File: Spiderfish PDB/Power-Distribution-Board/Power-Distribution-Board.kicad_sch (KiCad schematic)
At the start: 20 parts, among them J1 USB_B_Micro, J2 Conn_01x04_Pin, SW1 SW_Push, SW2 SW_SPDT, U1 STM32L052K6T6, U2 AOZ2264NQI-11

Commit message: added all regulators
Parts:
- added C10, C7: 330u, symbol Device:C
- added C11, C8: 10n, symbol Device:C
- added C12, C13, C14, C15, C16, C17, C18, C19, C20, C21, C22, C23, C24, C25, C26, C27, C28, C29, C30, C31: C, symbol Device:C
- added C6, C9: 100u, symbol Device:C
- added D1, D2: SK32, symbol Device:D
- added L2, L3: 33u, symbol Device:L
- added L4, L5, L6, L7, L8: L, symbol Device:L
- added R10, R12: 10k, symbol Device:R
- added R11: 17k, symbol Device:R
- added R13, R14, R15, R18, R19, R20, R23, R24, R25, R28, R29, R30, R33, R34, R35: R, symbol Device:R
- added R16, R31: 210k, symbol Device:R
- added R17, R27: 13k, symbol Device:R
- added R21, R36: 220k, symbol Device:R
- added R22, R37: 30k, symbol Device:R
- added R26: 247k, symbol Device:R
- added R32: 15k, symbol Device:R
- added R9: 31k, symbol Device:R
- added U3, U4: LM2596, Power_Distribution_Board:LM2596DSADJG, symbol Power_Distribution_Board:LM2596
- added U5, U6, U7, U8, U9: AOZ2264NQI-11, Power_Distribution_Board:AOZ2264NQI11, symbol Power_Distribution_Board:AOZ2264NQI-11
- R2: value R -> 247k
- R3: value R -> 13k
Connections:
- net +3V3: now also R1.1, U2.22 (IN_4), U2.24 (IN_5), U2.7 (IN_1), U2.8 (IN_2), U2.9 (IN_3), C10.1, C11.1, C11.2, L3.2, R11.1, R11.2, R12.1, R14.1, R19.1, R24.1, R29.1, R34.1, U4.4 (FEEDBACK), U5.22 (IN_4), U5.24 (IN_5), U5.7 (IN_1), U5.8 (IN_2), U5.9 (IN_3), U6.22 (IN_4), U6.24 (IN_5), U6.7 (IN_1), U6.8 (IN_2), U6.9 (IN_3), U7.22 (IN_4), U7.24 (IN_5), U7.7 (IN_1), U7.8 (IN_2), U7.9 (IN_3), U8.22 (IN_4), U8.24 (IN_5), U8.7 (IN_1), U8.8 (IN_2), U8.9 (IN_3), U9.22 (IN_4), U9.24 (IN_5), U9.7 (IN_1), U9.8 (IN_2), U9.9 (IN_3)
- net +5V: now also C12.1, C16.1, C20.1, C24.1, C28.1, C7.1, C8.1, C8.2, L2.2, R10.1, R15.1, R20.1, R25.1, R30.1, R35.1, R9.1, R9.2, U3.4 (FEEDBACK), U5.21 (VCC), U6.21 (VCC), U7.21 (VCC), U8.21 (VCC), U9.21 (VCC)
- net GND: now also C10.2, C12.2, C13.2, C16.2, C17.2, C20.2, C21.2, C24.2, C25.2, C28.2, C29.2, C6.2, C7.2, C9.2, D1.2 (A), D2.2 (A), R10.2, R12.2, R13.2, R17.2, R18.2, R22.2, R23.2, R27.2, R28.2, R32.2, R33.2, R37.2, U3.3 (GND), U3.5 (~ON/OFF), U4.3 (GND), U4.5 (~ON/OFF), U5.3 (MODE), U5.4 (AGND), U6.3 (MODE), U6.4 (AGND), U7.3 (MODE), U7.4 (AGND), U8.3 (MODE), U8.4 (AGND), U9.3 (MODE), U9.4 (AGND)
- net GNDPWR: now also C15.2, C19.2, C23.2, C27.2, C31.2, U5.12 (PGND_1), U5.13 (PGND_2), U5.14 (PGND_3), U5.15 (PGND_4), U6.12 (PGND_1), U6.13 (PGND_2), U6.14 (PGND_3), U6.15 (PGND_4), U7.12 (PGND_1), U7.13 (PGND_2), U7.14 (PGND_3), U7.15 (PGND_4), U8.12 (PGND_1), U8.13 (PGND_2), U8.14 (PGND_3), U8.15 (PGND_4), U9.12 (PGND_1), U9.13 (PGND_2), U9.14 (PGND_3), U9.15 (PGND_4)
- net at U1.10 (PA4): now also U8.2 (EN/DISCHG)
- net at U1.11 (PA5): now also U7.2 (EN/DISCHG)
- net at U1.6 (PA0): now also U6.2 (EN/DISCHG)
- net at U1.7 (PA1): now also U5.2 (EN/DISCHG)
- net at U1.8 (PA2): now also U2.2 (EN/DISCHG)
- net at U1.9 (PA3): now also U9.2 (EN/DISCHG)
- new net: D2.1 (K), L3.1, U4.2 (VOUT)
- new net: C23.1, L6.2, R26.1
- new net: R25.2, U7.1 (PGOOD)
- new net: R23.1, U7.19 (OCS)
- new net: C22.2, U7.20 (BST)
- new net: C21.1, U7.23 (SS)
- new net: R26.2, R27.1, U7.5 (FB)
- new net: R24.2, U7.6 (TON)
- new net: R19.2, U6.6 (TON)
- new net: R29.2, U8.6 (TON)
- new net: R30.2, U8.1 (PGOOD)
- new net: R28.1, U8.19 (OCS)
- new net: C26.2, U8.20 (BST)
- new net: C25.1, U8.23 (SS)
- new net: R31.2, R32.1, U8.5 (FB)
- new net: R15.2, U5.1 (PGOOD)
- new net: C31.1, L8.2, R36.1
- new net: R36.2, R37.1, U9.5 (FB)
- new net: C14.2, U5.20 (BST)
- new net: R20.2, U6.1 (PGOOD)
- new net: C13.1, U5.23 (SS)
- new net: C18.2, U6.20 (BST)
- new net: R35.2, U9.1 (PGOOD)
- new net: R18.1, U6.19 (OCS)
- new net: C17.1, U6.23 (SS)
- new net: R21.2, R22.1, U6.5 (FB)
- new net: R14.2, U5.6 (TON)
- new net: R13.1, U5.19 (OCS)
- new net: R16.2, R17.1, U5.5 (FB)
- new net: C19.1, L5.2, R21.1
- new net: D1.1 (K), L2.1, U3.2 (VOUT)
- new net: C15.1, L4.2, R16.1
- new net: R33.1, U9.19 (OCS)
- new net: C27.1, L7.2, R31.1
- new net: C30.2, U9.20 (BST)
- new net: C29.1, U9.23 (SS)
- new net: R34.2, U9.6 (TON)
- new net +14V8: C6.1, C9.1, U3.1 (VIN), U4.1 (VIN)
- new net LX12V_2: C22.1, L6.1, U7.10 (LX_1), U7.11 (LX_2), U7.16 (LX_3), U7.17 (LX_4), U7.18 (LX_5), U7.25 (LX_6)
- new net LX5V_1: C18.1, L5.1, U6.10 (LX_1), U6.11 (LX_2), U6.16 (LX_3), U6.17 (LX_4), U6.18 (LX_5), U6.25 (LX_6)
- new net LX5V_2: C30.1, L8.1, U9.10 (LX_1), U9.11 (LX_2), U9.16 (LX_3), U9.17 (LX_4), U9.18 (LX_5), U9.25 (LX_6)
- new net LX9V_1: C14.1, L4.1, U5.10 (LX_1), U5.11 (LX_2), U5.16 (LX_3), U5.17 (LX_4), U5.18 (LX_5), U5.25 (LX_6)
- new net LX9V_2: C26.1, L7.1, U8.10 (LX_1), U8.11 (LX_2), U8.16 (LX_3), U8.17 (LX_4), U8.18 (LX_5), U8.25 (LX_6)
- no-connect marks 2 -> 16
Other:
- moved on the sheet: C1, C2, C3, C4, C5, J1, J2, L1, R1, R2, R3, R4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

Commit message: added footprints and p/n
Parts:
- removed C1, C13, C2, C3: C, symbol Device:C
- removed L1: L, symbol Device:L
- removed L2, L3: 33u, symbol Device:L
- removed R1, R15, R20, R30, R35, R5: R, symbol Device:R
- removed R12: 10k, symbol Device:R
- removed R2: 247k, symbol Device:R
- removed R3: 13k, symbol Device:R
- removed R32: 15k, symbol Device:R
- removed R8: 10K, symbol Device:R
- removed SW1: SW_Push, symbol Switch:SW_Push
- removed SW2: SW_SPDT, symbol Switch:SW_SPDT
- added C32, C33: 100n, Capacitor_SMD:C_1206_3216Metric_Pad1.33x1.80mm_HandSolder, symbol Device:C
- added C34: 10u, Capacitor_SMD:C_0805_2012Metric_Pad1.18x1.45mm_HandSolder, symbol Device:C
- added C4: 100u, Capacitor_SMD:C_1210_3225Metric_Pad1.33x2.70mm_HandSolder, symbol Device:C
- added C5: 10n, Capacitor_SMD:C_0805_2012Metric_Pad1.18x1.45mm_HandSolder, symbol Device:C
- added C6: 470u, Capacitor_THT:CP_Radial_D8.0mm_P3.50mm, symbol Device:C
- added C8: 22u, Capacitor_SMD:C_0805_2012Metric_Pad1.18x1.45mm_HandSolder, symbol Device:C
- added L1, L2: 33u, Power_Distribution_Board:SRP1038A-470M, symbol Power_Distribution_Board:SRP1038A-470M
- added L6: 2u2, Power_Distribution_Board:SRP1265A-2R2M, symbol Device:L
- added R11: 499k, Resistor_SMD:R_0805_2012Metric_Pad1.20x1.40mm_HandSolder, symbol Device:R
- added R14, R26: 20k, Resistor_SMD:R_0805_2012Metric_Pad1.20x1.40mm_HandSolder, symbol Device:R
- added R19, R9: 100k, Resistor_SMD:R_0805_2012Metric_Pad1.20x1.40mm_HandSolder, symbol Device:R
- added R21: 374k, Resistor_SMD:R_0805_2012Metric_Pad1.20x1.40mm_HandSolder, symbol Device:R
- added R24: 182k, Resistor_SMD:R_0805_2012Metric_Pad1.20x1.40mm_HandSolder, symbol Device:R
- added R25, R27: 13k, Resistor_SMD:R_0805_2012Metric_Pad1.20x1.40mm_HandSolder, symbol Device:R
- added R4, R7: 10k, Resistor_SMD:R_0805_2012Metric_Pad1.20x1.40mm_HandSolder, symbol Device:R
- added S1: TR1-01, Power_Distribution_Board:TR101, symbol Power_Distribution_Board:TR1-01
- added S2: EG1218, Power_Distribution_Board:EG1218, symbol Power_Distribution_Board:EG1218
- added U4: USBLC6-2SC6, Power_Distribution_Board:USBLC6-2SC6, symbol Power_Distribution_Board:USBLC6-2SC6
- C1: renamed from C6; footprint (none) -> Capacitor_SMD:C_1210_3225Metric_Pad1.33x2.70mm_HandSolder; Model (none) -> EMK325ABJ107MM-P
- C10: value 330u -> 100n; footprint (none) -> Capacitor_SMD:C_1206_3216Metric_Pad1.33x1.80mm_HandSolder; Model (none) -> GRM3195C2A104GA01D
- C11: value 10n -> 100n; footprint (none) -> Capacitor_SMD:C_1206_3216Metric_Pad1.33x1.80mm_HandSolder; Model (none) -> GRM3195C2A104GA01D
- C12, C20, C22, C28, C30: value C -> 4u7; footprint (none) -> Capacitor_SMD:C_0805_2012Metric_Pad1.18x1.45mm_HandSolder; Model (none) -> C0805C475J3RACTU
- C13: renamed from C4; value C -> 4u7; footprint (none) -> Capacitor_SMD:C_0805_2012Metric_Pad1.18x1.45mm_HandSolder; Model (none) -> C0805C475J3RACTU
- C14, C15, C21, C23, C29, C31: value C -> 10n; footprint (none) -> Capacitor_SMD:C_0805_2012Metric_Pad1.18x1.45mm_HandSolder; Model (none) -> 0805N103F500CT
- C16, C17, C24, C25: value C -> 22u; footprint (none) -> Capacitor_SMD:C_0805_2012Metric_Pad1.18x1.45mm_HandSolder; Model (none) -> CL21A226KQCLRNC
- C18, C19, C26, C27: value C -> 100n; footprint (none) -> Capacitor_SMD:C_1206_3216Metric_Pad1.33x1.80mm_HandSolder; Model (none) -> GRM3195C2A104GA01D
- C2: renamed from C8; footprint (none) -> Capacitor_SMD:C_0805_2012Metric_Pad1.18x1.45mm_HandSolder; Model (none) -> 0805N103F500CT
- C3: renamed from C7; value 330u -> 470u; footprint (none) -> Capacitor_THT:CP_Radial_D8.0mm_P3.50mm; Model (none) -> ESY477M016AG8AA
- C7: renamed from C5; footprint (none) -> Capacitor_SMD:C_1206_3216Metric_Pad1.33x1.80mm_HandSolder; Model (none) -> GRM3195C2A104GA01D
- C9: value 100u -> 22u; footprint (none) -> Capacitor_SMD:C_0805_2012Metric_Pad1.18x1.45mm_HandSolder; Model (none) -> CL21A226KQCLRNC
- D1, D2: footprint (none) -> Diode_SMD:D_SMC
- J1: renamed from J2; footprint (none) -> Connector_PinHeader_2.54mm:PinHeader_1x04_P2.54mm_Vertical; Model (none) -> 61300411121
- J2: renamed from J1; footprint (none) -> Connector_USB:USB_Micro-B_Wuerth_629105150521; Model (none) -> 629105150521
- L3: renamed from L6; value L -> 2u2; footprint (none) -> Power_Distribution_Board:SRP1265A-2R2M; Model (none) -> SRP1265A-2R2M
- L4, L5, L7, L8: value L -> 2u2; footprint (none) -> Power_Distribution_Board:SRP1265A-2R2M; Model (none) -> SRP1265A-2R2M
- R1: renamed from R10; footprint (none) -> Resistor_SMD:R_0805_2012Metric_Pad1.20x1.40mm_HandSolder; Model (none) -> RG2012P-103-B-T5
- R10: renamed from R24; value R -> 499k; footprint (none) -> Resistor_SMD:R_0805_2012Metric_Pad1.20x1.40mm_HandSolder; Model (none) -> ERA-6AEB4993V
- R12: renamed from R26; value 247k -> 249k; footprint (none) -> Resistor_SMD:R_0805_2012Metric_Pad1.20x1.40mm_HandSolder; Model (none) -> ERA-6AEB2493V
- R13: value R -> 249k; footprint (none) -> Resistor_SMD:R_0805_2012Metric_Pad1.20x1.40mm_HandSolder; Model (none) -> ERA-6AEB2493V
- R15: renamed from R4; value R -> 20k; footprint (none) -> Resistor_SMD:R_0805_2012Metric_Pad1.20x1.40mm_HandSolder; Model (none) -> ERA-6AEB203V
- R16: renamed from R27; footprint (none) -> Resistor_SMD:R_0805_2012Metric_Pad1.20x1.40mm_HandSolder; Model (none) -> ERA-6AEB133V
- R17: footprint (none) -> Resistor_SMD:R_0805_2012Metric_Pad1.20x1.40mm_HandSolder; Model (none) -> ERA-6AEB133V
- R18, R28, R29: value R -> 100k; footprint (none) -> Resistor_SMD:R_0805_2012Metric_Pad1.20x1.40mm_HandSolder; Model (none) -> ERA-6AEB104V
- R2: renamed from R9; value 31k -> 30k; footprint (none) -> Resistor_SMD:R_0805_2012Metric_Pad1.20x1.40mm_HandSolder; Model (none) -> ERA-6AEB303V
- R20: renamed from R14; value R -> 374k; footprint (none) -> Resistor_SMD:R_0805_2012Metric_Pad1.20x1.40mm_HandSolder; Model (none) -> ERA-6AEB3743V
- R22: renamed from R16; value 210k -> 182k; footprint (none) -> Resistor_SMD:R_0805_2012Metric_Pad1.20x1.40mm_HandSolder; Model (none) -> ERA-6AEB1823V
- R23, R33: value R -> 20k; footprint (none) -> Resistor_SMD:R_0805_2012Metric_Pad1.20x1.40mm_HandSolder; Model (none) -> ERA-6AEB203V
- R3: renamed from R7; footprint (none) -> Resistor_SMD:R_0805_2012Metric_Pad1.20x1.40mm_HandSolder; Model (none) -> ERA-6AEB823V
- R30: renamed from R19; value R -> 205k; footprint (none) -> Resistor_SMD:R_0805_2012Metric_Pad1.20x1.40mm_HandSolder; Model (none) -> ERA-6AEB2053V
- R31: value 210k -> 205k; footprint (none) -> Resistor_SMD:R_0805_2012Metric_Pad1.20x1.40mm_HandSolder; Model (none) -> ERA-6AEB2053V
- R32: renamed from R21; footprint (none) -> Resistor_SMD:R_0805_2012Metric_Pad1.20x1.40mm_HandSolder; Model (none) -> ERA-6AEB224V
- R34: value R -> 220k; footprint (none) -> Resistor_SMD:R_0805_2012Metric_Pad1.20x1.40mm_HandSolder; Model (none) -> ERA-6AEB224V
- R35: renamed from R22; footprint (none) -> Resistor_SMD:R_0805_2012Metric_Pad1.20x1.40mm_HandSolder; Model (none) -> ERA-6AEB303V
- R36: value 220k -> 20k; footprint (none) -> Resistor_SMD:R_0805_2012Metric_Pad1.20x1.40mm_HandSolder; Model (none) -> ERA-6AEB203V
- R37: footprint (none) -> Resistor_SMD:R_0805_2012Metric_Pad1.20x1.40mm_HandSolder; Model (none) -> ERA-6AEB303V
- R5: renamed from R6; footprint (none) -> Resistor_SMD:R_0805_2012Metric_Pad1.20x1.40mm_HandSolder; Model (none) -> ERA-6AEB333V
- R6: renamed from R11; value 17k -> 17k2; footprint (none) -> Resistor_SMD:R_0603_1608Metric_Pad0.98x0.95mm_HandSolder; Model (none) -> RN73R1JTTD1722B25
- R8: renamed from R25; value R -> 100k; footprint (none) -> Resistor_SMD:R_0805_2012Metric_Pad1.20x1.40mm_HandSolder; Model (none) -> ERA-6AEB104V
- renumbered U9 to U10, U3 to U2, U4 to U3, U7 to U5, U2 to U6, U5 to U7, U6 to U9
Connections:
- net +14V8: now also C4.1; no longer C9.1
- net +3V3: now also R31.1, C32.1, C33.1, C34.1, C5.1, C5.2, C6.1, L2.2, R11.1, R21.1, R4.1, S2.3 (NO); no longer C10.1, C11.1, C11.2, R29.1, R34.1
- net +5V: now also C17.1, C25.1, C9.1, R18.1, R28.1, R29.1, C8.1, L1.2, R19.1, R9.1; no longer C12.1, C20.1, C28.1
- net BOOT0: now also R7.2
- net GND: now also C14.2, C15.2, C23.2, C31.2, R36.2, C32.2, C33.2, C34.2, C4.2, C6.2, C8.2, R14.2, R25.2, R26.2, R27.2, R4.2, S1.1 (COM_1), S1.2 (COM_2), S2.1 (NC), U4.2 (GND); no longer C10.2, C12.2, C20.2, C28.2, R13.2, R18.2, R28.2
- net GNDPWR: now also C12.2, C20.2, C22.2, C28.2, C30.2; no longer C15.2, C19.2, C23.2, C27.2, C31.2
- net LX12V_1: now also C11.2, L4.1
- net LX12V_2: now also C10.2; no longer C22.1
- net LX5V_1: now also C26.2, L7.1; no longer C18.1, L5.1
- net LX5V_2: now also C27.2; no longer C30.1
- net LX9V_1: now also C18.2, L5.1; no longer C14.1, L4.1
- net LX9V_2: now also C19.2, L6.1; no longer C26.1, L7.1
- net NRST: now also S1.3 (NO_1), S1.4 (NO_2)
- net SW_BOOT0: now also R7.1, S2.2 (COMM)
- net USB_D+: now also U4.3 (I/O2_1); no longer J2.3 (D+)
- net USB_D-: now also U4.1 (I/O1_1); no longer J2.2 (D-)
- net at D2.1 (K), U3.2 (VOUT): now also L2.1
- net at L3.2, R12.1: now also C12.1; no longer C23.1
- net at U5.19 (OCS): now also R14.1; no longer R23.1
- net at U5.20 (BST): now also C10.1; no longer C22.2
- net at U5.23 (SS): now also C14.1; no longer C21.1
- net at U8.6 (TON): now also R21.2; no longer R29.2
- net at U8.1 (PGOOD): now also R19.2
- net at U6.5 (FB): now also R13.2, R17.1
- net at U8.19 (OCS): now also R26.1; no longer R28.1
- net at U8.20 (BST): now also C19.1; no longer C26.2
- net at U8.23 (SS): now also C23.1; no longer C25.1
- net at U8.5 (FB): now also R24.2, R27.1; no longer R31.2
- net at U6.6 (TON): now also R11.2
- net at U6.20 (BST): now also C11.1
- net at U7.1 (PGOOD): now also R18.2
- net at R37.1, U10.5 (FB): now also R34.2; no longer R36.2
- net at U7.20 (BST): now also C18.1; no longer C14.2
- net at U9.1 (PGOOD): now also R28.2
- net at U7.23 (SS): now also C21.1
- net at U9.20 (BST): now also C26.1; no longer C18.2
- net at U10.1 (PGOOD): now also R29.2
- net at U6.1 (PGOOD): now also R9.2
- net at U6.23 (SS): now also C15.1
- net at U9.19 (OCS): now also R33.1; no longer R18.1
- net at U9.23 (SS): now also C29.1; no longer C17.1
- net at U7.19 (OCS): now also R23.1; no longer R13.1
- net at R22.2, U7.5 (FB): now also R25.1; no longer R17.1
- net at J2.1 (VBUS), R5.1: now also U4.5 (VBUS)
- net at C13.1: now also L4.2, R13.1
- net at D1.1 (K), U2.2 (VOUT): now also L1.1
- net at U10.19 (OCS): now also R36.1; no longer R33.1
- net at U10.20 (BST): now also C27.1; no longer C30.2
- net at U10.23 (SS): now also C31.1; no longer C29.1
- net at U10.6 (TON): now also R31.2; no longer R34.2
- new net: C28.1, L7.2, R32.1
- new net: C20.1, L5.2, R22.1
- new net: C22.1, L6.2, R24.1
- new net: J2.3 (D+), U4.4 (I/O2_2)
- new net: J2.2 (D-), U4.6 (I/O1_2)
- new net: C30.1, L8.2, R34.1
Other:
- moved on the sheet: J2, R16, R20, R22, R3, R30, R32, R35, R5, U10, U7, U8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

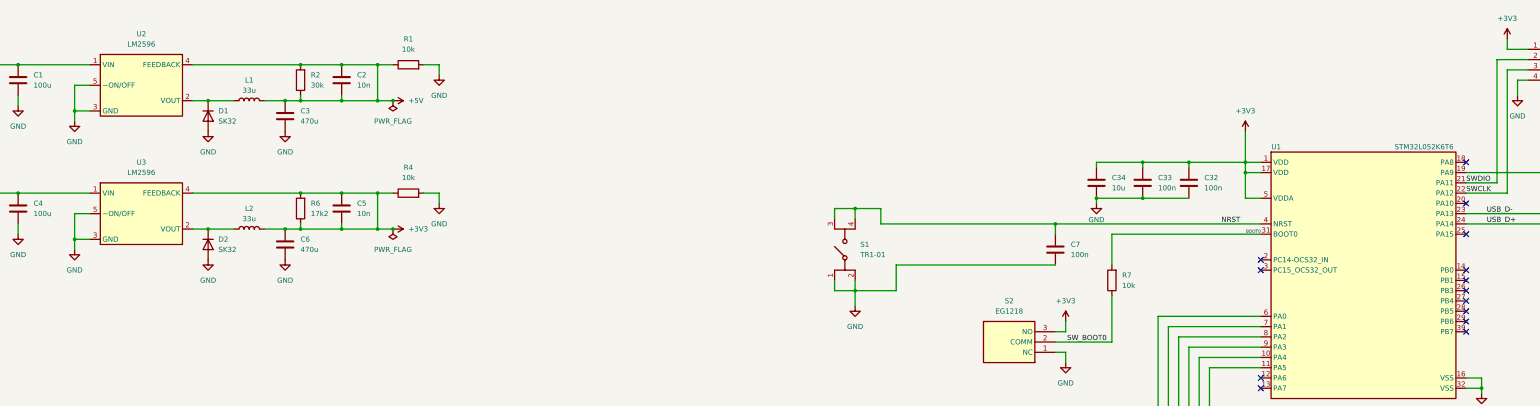
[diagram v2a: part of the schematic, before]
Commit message: changed resistor package to 0603 from 0805
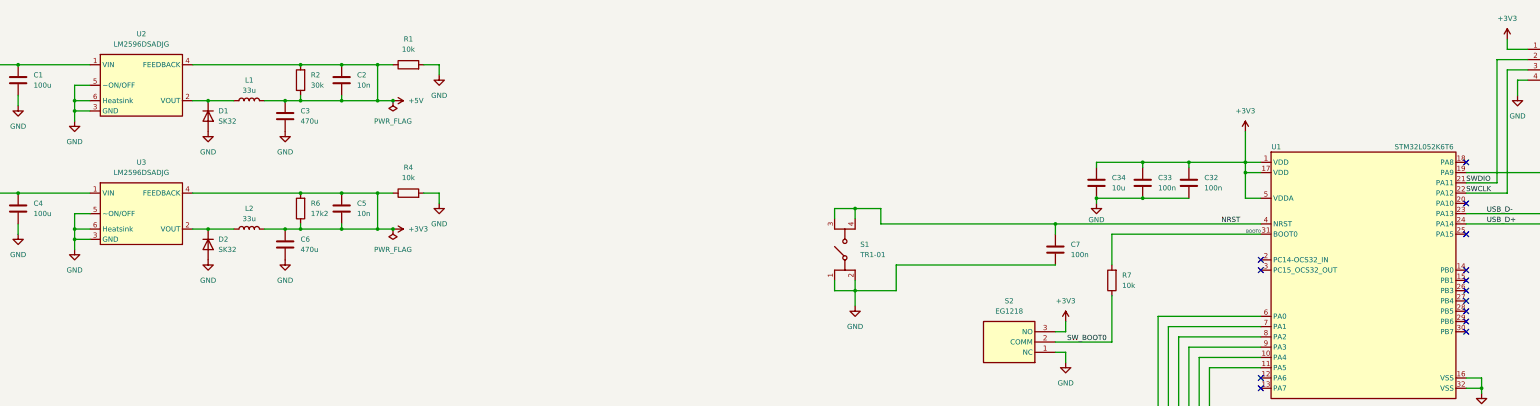
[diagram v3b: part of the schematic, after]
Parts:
- removed U2, U3: LM2596, Power_Distribution_Board:LM2596DSADJG, symbol Power_Distribution_Board:LM2596
- added U2, U3: LM2596DSADJG, Power_Distribution_Board:LM2596DSADJG, symbol Power_Distribution_Board:LM2596DSADJG
- R1, R4, R7: footprint Resistor_SMD:R_0805_2012Metric_Pad1.20x1.40mm_HandSolder -> Resistor_SMD:R_0603_1608Metric_Pad0.98x0.95mm_HandSolder; Model RG2012P-103-B-T5 -> ERJ-PB3B1002V
- R10, R11: footprint Resistor_SMD:R_0805_2012Metric_Pad1.20x1.40mm_HandSolder -> Resistor_SMD:R_0603_1608Metric_Pad0.98x0.95mm_HandSolder; Model ERA-6AEB4993V -> RN73H1JTTD4993B25
- R12, R13: footprint Resistor_SMD:R_0805_2012Metric_Pad1.20x1.40mm_HandSolder -> Resistor_SMD:R_0603_1608Metric_Pad0.98x0.95mm_HandSolder; Model ERA-6AEB2493V -> TNPW0603249KBEEA
- R14, R15, R23, R26, R33, R36: footprint Resistor_SMD:R_0805_2012Metric_Pad1.20x1.40mm_HandSolder -> Resistor_SMD:R_0603_1608Metric_Pad0.98x0.95mm_HandSolder; Model ERA-6AEB203V -> ERJ-PB3B2002V
- R16, R17, R25, R27: footprint Resistor_SMD:R_0805_2012Metric_Pad1.20x1.40mm_HandSolder -> Resistor_SMD:R_0603_1608Metric_Pad0.98x0.95mm_HandSolder; Model ERA-6AEB133V -> ERJ-PB3B1302V
- R18, R19, R28, R29, R8, R9: footprint Resistor_SMD:R_0805_2012Metric_Pad1.20x1.40mm_HandSolder -> Resistor_SMD:R_0603_1608Metric_Pad0.98x0.95mm_HandSolder; Model ERA-6AEB104V -> ERJ-PB3B1003V
- R2: footprint Resistor_SMD:R_0805_2012Metric_Pad1.20x1.40mm_HandSolder -> Resistor_SMD:R_0603_1608Metric_Pad0.98x0.95mm_HandSolder; Model ERA-6AEB303V -> ERJ-PB3B3002V
- R20, R21: footprint Resistor_SMD:R_0805_2012Metric_Pad1.20x1.40mm_HandSolder -> Resistor_SMD:R_0603_1608Metric_Pad0.98x0.95mm_HandSolder; Model ERA-6AEB3743V -> RT0603BRD07374KL
- R22, R24: footprint Resistor_SMD:R_0805_2012Metric_Pad1.20x1.40mm_HandSolder -> Resistor_SMD:R_0603_1608Metric_Pad0.98x0.95mm_HandSolder; Model ERA-6AEB1823V -> ERA-3AEB1823V
- R3: footprint Resistor_SMD:R_0805_2012Metric_Pad1.20x1.40mm_HandSolder -> Resistor_SMD:R_0603_1608Metric_Pad0.98x0.95mm_HandSolder; Model ERA-6AEB823V -> ERJ-PB3B8202V
- R30, R31: footprint Resistor_SMD:R_0805_2012Metric_Pad1.20x1.40mm_HandSolder -> Resistor_SMD:R_0603_1608Metric_Pad0.98x0.95mm_HandSolder; Model ERA-6AEB2053V -> TNPW0603205KBEEA
- R32, R34: footprint Resistor_SMD:R_0805_2012Metric_Pad1.20x1.40mm_HandSolder -> Resistor_SMD:R_0603_1608Metric_Pad0.98x0.95mm_HandSolder; Model ERA-6AEB224V -> RNCF0603BTE220K
- R35, R37: footprint Resistor_SMD:R_0805_2012Metric_Pad1.20x1.40mm_HandSolder -> Resistor_SMD:R_0603_1608Metric_Pad0.98x0.95mm_HandSolder; Model ERA-6AEB303V -> RNCF0603BTE30K0
- R5: footprint Resistor_SMD:R_0805_2012Metric_Pad1.20x1.40mm_HandSolder -> Resistor_SMD:R_0603_1608Metric_Pad0.98x0.95mm_HandSolder; Model ERA-6AEB333V -> ERJ-PB3B3302V
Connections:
- net +14V8: now also U2.1 (VIN), U3.1 (VIN)
- net +3V3: now also U3.4 (FEEDBACK)
- net +5V: now also U2.4 (FEEDBACK)
- net GND: now also U2.3 (GND), U2.5 (~ON/OFF), U2.6 (Heatsink), U3.3 (GND), U3.5 (~ON/OFF), U3.6 (Heatsink)
- net at D1.1 (K), L1.1: now also U2.2 (VOUT)
- net at D2.1 (K), L2.1: now also U3.2 (VOUT)

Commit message: added connectors
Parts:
- added J3, J4, J5, J6, J7, J8: TB002-500-02BE, Power_Distribution_Board:TB002-500-02BE, symbol Power_Distribution_Board:TB002-500-02BE
- added J9: XT90PW-F, Power_Distribution_Board:XT90PWF, symbol Power_Distribution_Board:XT90PW-F
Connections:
- net +14V8: now also J9.1 (+)
- net GND: now also J9.2 (-)
- net GNDPWR: now also J3.2, J4.2, J5.2, J6.2, J7.2, J8.2
- net at C28.1, L7.2, R32.1: now also J7.1
- net at C20.1, L5.2, R22.1: now also J5.1
- net at C12.1, L3.2, R12.1: now also J4.1
- net at C22.1, L6.2, R24.1: now also J6.1
- net at C13.1, L4.2, R13.1: now also J3.1
- net at C30.1, L8.2, R34.1: now also J8.1
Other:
- moved on the sheet: C1, C2, C3, C4, C5, C6, D1, D2, L1, L2, R1, R2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

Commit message: added net labels
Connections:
- net +3V3: no longer C5.1, R4.1, R6.2, U3.4 (FEEDBACK)
- net +5V: no longer C2.1, R1.1, R2.2, U2.4 (FEEDBACK)
- net 12V_OSC_1: now reaches R15.1, U6.19 (OCS)
- net 5V_L: now reaches D1.1 (K), L1.1, U2.2 (VOUT)
- net 12V_PGOOD_2: now reaches R8.2, U5.1 (PGOOD)
- net 12V_OSC_2: now reaches R14.1, U5.19 (OCS)
- net 12V_EN_2: now reaches U1.11 (PA5), U5.2 (EN/DISCHG)
- net 12V_SS_2: now reaches C14.1, U5.23 (SS)
- net 12V_FB_2: now reaches R12.2, R16.1, U5.5 (FB)
- net 12V_FB_2: now also R13.2, R17.1, U6.5 (FB)
- net 12V_TON_2: now reaches R10.2, U5.6 (TON)
- net USB_ACK: now reaches R3.1, R5.2, U1.19 (PA9)
- net 12V_OUT_2: now reaches C12.1, J4.1, L3.2, R12.1
- net 9V_EN_2: now reaches U1.10 (PA4), U8.2 (EN/DISCHG)
- net 12V_OUT1: now reaches C13.1, J3.1, L4.2, R13.1
- net USB_USB_D+: now reaches J2.3 (D+), U4.4 (I/O2_2)
- net USB_VBUS: now reaches J2.1 (VBUS), R5.1, U4.5 (VBUS)
- net USB_USB_D-: now reaches J2.2 (D-), U4.6 (I/O1_2)
- net 5V_EN_1: now reaches U1.6 (PA0), U9.2 (EN/DISCHG)
- net 9V_EN_1: now reaches U1.7 (PA1), U7.2 (EN/DISCHG)
- net 12V_EN_1: now reaches U1.8 (PA2), U6.2 (EN/DISCHG)
- net 5V_EN_2: now reaches U1.9 (PA3), U10.2 (EN/DISCHG)
- net 12V_PGOOD_1: now reaches R9.2, U6.1 (PGOOD)
- net 12V_SS_1: now reaches C15.1, U6.23 (SS)
- net 12V_TON_1: now reaches R11.2, U6.6 (TON)
- net LX12V_1 renamed 12V_LX_1
- net LX12V_2 renamed 12V_LX_2
- new net 3V3_FB: C5.1, R4.1, R6.2, U3.4 (FEEDBACK)
- new net 5V_FB: C2.1, R1.1, R2.2, U2.4 (FEEDBACK)
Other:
- moved on the sheet: R10, R11

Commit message: finished adding labels and net classes
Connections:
- net +14V8: now also R10.1, R11.1, R20.1, R21.1, R30.1, R31.1, U10.22 (IN_4), U10.24 (IN_5), U10.7 (IN_1), U10.8 (IN_2), U10.9 (IN_3), U5.22 (IN_4), U5.24 (IN_5), U5.7 (IN_1), U5.8 (IN_2), U5.9 (IN_3), U6.22 (IN_4), U6.24 (IN_5), U6.7 (IN_1), U6.8 (IN_2), U6.9 (IN_3), U7.22 (IN_4), U7.24 (IN_5), U7.7 (IN_1), U7.8 (IN_2), U7.9 (IN_3), U8.22 (IN_4), U8.24 (IN_5), U8.7 (IN_1), U8.8 (IN_2), U8.9 (IN_3), U9.22 (IN_4), U9.24 (IN_5), U9.7 (IN_1), U9.8 (IN_2), U9.9 (IN_3)
- net +3V3: no longer R10.1, R11.1, R20.1, R21.1, R30.1, R31.1, U10.22 (IN_4), U10.24 (IN_5), U10.7 (IN_1), U10.8 (IN_2), U10.9 (IN_3), U5.22 (IN_4), U5.24 (IN_5), U5.7 (IN_1), U5.8 (IN_2), U5.9 (IN_3), U6.22 (IN_4), U6.24 (IN_5), U6.7 (IN_1), U6.8 (IN_2), U6.9 (IN_3), U7.22 (IN_4), U7.24 (IN_5), U7.7 (IN_1), U7.8 (IN_2), U7.9 (IN_3), U8.22 (IN_4), U8.24 (IN_5), U8.7 (IN_1), U8.8 (IN_2), U8.9 (IN_3), U9.22 (IN_4), U9.24 (IN_5), U9.7 (IN_1), U9.8 (IN_2), U9.9 (IN_3)
- net 12V_FB_2: no longer R13.2, R17.1, U6.5 (FB)
- net 12V_PGOOD_1: now also U1.14 (PB0)
- net 12V_PGOOD_2: now also U1.15 (PB1)
- net 5V_OUT_1: now reaches C28.1, J7.1, L7.2, R32.1
- net 5V_BST_1: now reaches C26.1, U9.20 (BST)
- net 12V_BST_2: now reaches C10.1, U5.20 (BST)
- net 9V_OUT_1: now reaches C20.1, J5.1, L5.2, R22.1
- net 12V_BST_1: now reaches C11.1, U6.20 (BST)
- net 9V_PGOOD_2: now reaches R19.2, U8.1 (PGOOD)
- net 9V_PGOOD_2: now also U1.27 (PB4)
- net 9V_OSC_2: now reaches R26.1, U8.19 (OCS)
- net 9V_BST_2: now reaches C19.1, U8.20 (BST)
- net 9V_SS_2: now reaches C23.1, U8.23 (SS)
- net 9V_FB_2: now reaches R24.2, R27.1, U8.5 (FB)
- net 9V_TON_2: now reaches R21.2, U8.6 (TON)
- net 9V_OUT_2: now reaches C22.1, J6.1, L6.2, R24.1
- net 5V_SS_1: now reaches C29.1, U9.23 (SS)
- net 5V_OUT_2: now reaches C30.1, J8.1, L8.2, R34.1
- net 9V_PGOOD_1: now reaches U1.26 (PB3)
- net 9V_PGOOD_1: now also R18.2, U7.1 (PGOOD)
- net 5V_PGOOD_1: now reaches U1.28 (PB5)
- net 5V_PGOOD_1: now also R28.2, U9.1 (PGOOD)
- net 5V_PGOOD_2: now reaches U1.29 (PB6)
- net 5V_PGOOD_2: now also R29.2, U10.1 (PGOOD)
- net 5V_SS_2: now reaches C31.1, U10.23 (SS)
- net 9V_FB_1: now reaches R22.2, R25.1, U7.5 (FB)
- net 5V_FB_2: now reaches R34.2, R37.1, U10.5 (FB)
- net 9V_SS_1: now reaches C21.1, U7.23 (SS)
- net 5V_OSC_1: now reaches R33.1, U9.19 (OCS)
- net 5V_FB_1: now reaches R32.2, R35.1, U9.5 (FB)
- net 5V_TON_1: now reaches R30.2, U9.6 (TON)
- net 5V_BST_2: now reaches C27.1, U10.20 (BST)
- net 9V_TON_1: now reaches R20.2, U7.6 (TON)
- net 9V_OSC_1: now reaches R23.1, U7.19 (OCS)
- net 9V_BST_1: now reaches C18.1, U7.20 (BST)
- net 5V_OSC_2: now reaches R36.1, U10.19 (OCS)
- net 5V_TON_2: now reaches R31.2, U10.6 (TON)
- net LX5V_1 renamed 5V_LX_1
- net LX5V_2 renamed 5V_LX_2
- net LX9V_1 renamed 9V_LX_1
- net LX9V_2 renamed 9V_LX_2
- new net 12V_FB_1: R13.2, R17.1, U6.5 (FB)
- no-connect marks 16 -> 10
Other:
- moved on the sheet: C10, C11, C12, C13, C18, C19, C20, C22, C26, C27, C28, C30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

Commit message: added base design constraints and grouped pcb components
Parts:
- added C35, C36, C37, C38, C39, C40: 4u7, Capacitor_SMD:C_0805_2012Metric_Pad1.18x1.45mm_HandSolder, symbol Device:C
- J2: footprint Connector_USB:USB_Micro-B_Wuerth_629105150521 -> Power_Distribution_Board:629105150521
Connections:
- net +14V8: now also C16.1, C17.1, C24.1, C25.1, C8.1, C9.1
- net +5V: now also C35.1, C36.1, C37.1, C38.1, C39.1, C40.1; no longer C16.1, C17.1, C24.1, C25.1, C8.1, C9.1
- net GND: now also C35.2, C36.2, C37.2, C38.2, C39.2, C40.2
- net USB_D+: now also U4.1 (I/O1_1); no longer U4.3 (I/O2_1)
- net USB_D-: now also U4.3 (I/O2_1); no longer U4.1 (I/O1_1)
- net USB_USB_D+: now also U4.6 (I/O1_2); no longer U4.4 (I/O2_2)
- net USB_USB_D-: now also U4.4 (I/O2_2); no longer U4.6 (I/O1_2)
- net 3V3_L: now reaches D2.1 (K), L2.1, U3.2 (VOUT)
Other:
- moved on the sheet: C16, C17, C24, C25, C8, C9, R10, R21
